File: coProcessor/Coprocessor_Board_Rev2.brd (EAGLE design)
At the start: 101.6 x 101.6 mm, 95 parts, among them IC1 STM32F405RGT6, J1 USB_MINI-B_SMT, J4 30320-6002HB, J5 5008730806, Q1 L78M05CV, U1 MAX3051ESA

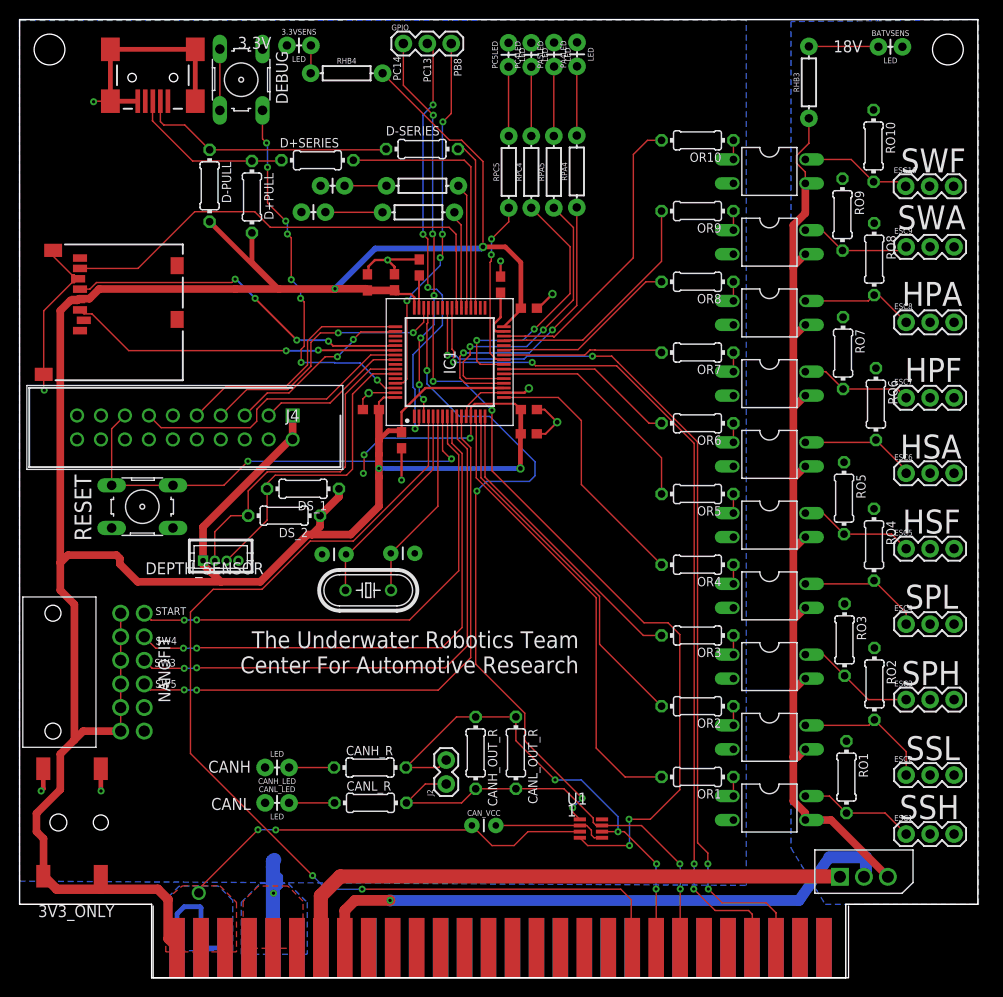
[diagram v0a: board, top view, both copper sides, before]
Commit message: fixed led orientation, added switch to switch connector
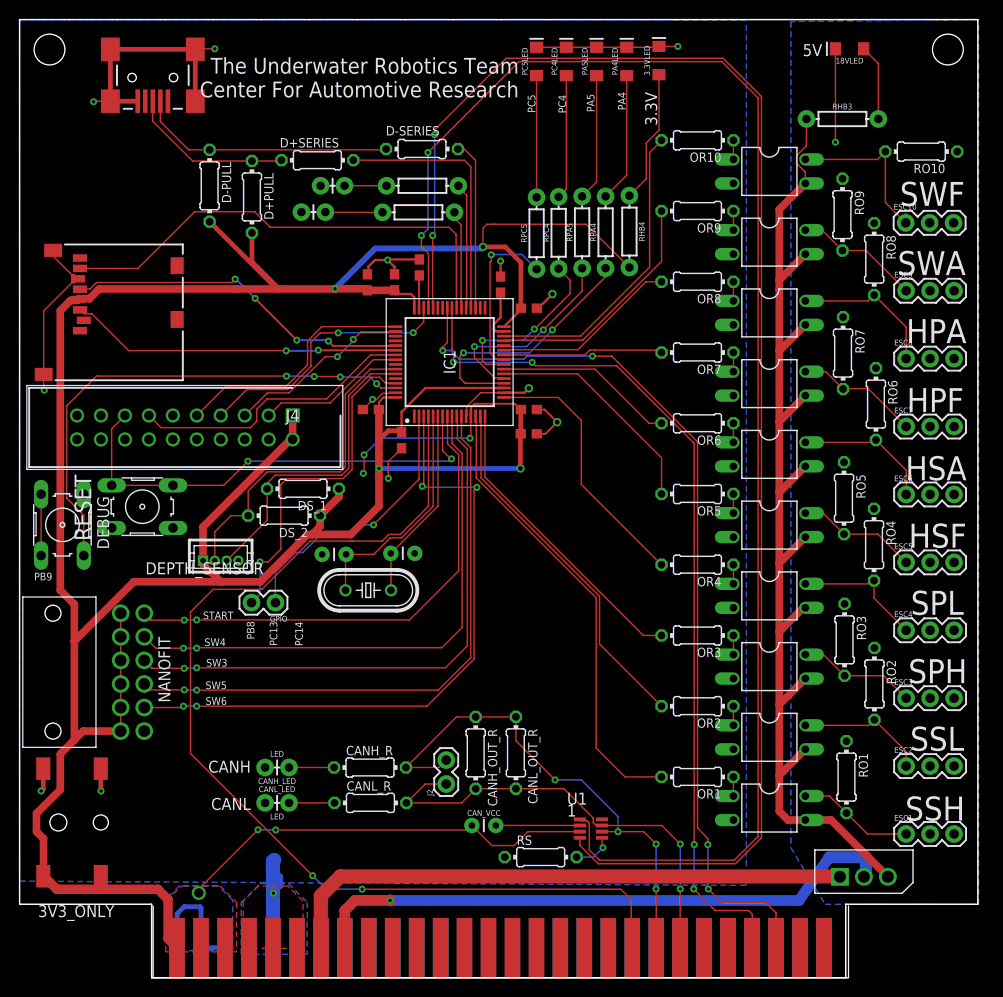
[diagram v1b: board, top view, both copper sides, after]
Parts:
- removed 3.3VSENS, BATVSENS: LED, SparkFun-Resistors:AXIAL-0.1
- added 18VLED, 3.3VLED: WHITE, SparkFun-LED:LED-1206
- added RS: 0, resistor:0204/7
- C10, C2, C3, C4, C5: value 100 nF -> .1 uF
- GPIO: device SparkFun-Connectors:1X03 -> SparkFun-Connectors:1X02
- PA4LED, PA5LED, PC4LED, PC5LED: value LED -> WHITE; device SparkFun-Resistors:AXIAL-0.1 -> SparkFun-LED:LED-1206
- RHB3: value 1.5k -> 1.8k
- RHB4, RPA4, RPA5, RPC4, RPC5: value 1k -> 330
- moved GPIO 60.8 mm to (27.1, 39.8), turned to 180 degrees
- moved DEBUG 50.9 mm to (4.54, 48.0)
- moved RHB4 34.4 mm to (64.7, 79.1), turned to 270 degrees
- moved RPC5 7.14 mm to (54.8, 78.9)
- moved RPA4 7.13 mm to (62.1, 79.0)
- moved RPC4 7.07 mm to (57.2, 79.0)
- moved RPA5 7.07 mm to (59.6, 79.0)
- moved PA4LED 5.33 mm to (64.4, 97.2)
- moved RHB3 5.26 mm to (87.2, 91.1), turned to 0 degrees
- moved RO10 5.10 mm to (95.6, 87.6), turned to 180 degrees
- moved ESC9 4.65 mm to (94.0, 72.8)
- moved PA5LED 4.57 mm to (61.2, 97.2)
- moved ESC10 3.88 mm to (93.9, 80.0)
- moved ESC8 3.85 mm to (94.0, 65.7)
- moved PC4LED 3.78 mm to (58.0, 97.2)
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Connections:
- net N$12 renamed PB9
- removed net GNDA: BATVSENS.P$2
- removed net PC14: GPIO.1, IC1.3
- new net N$2: RS.2, U1.8
- new net SWITCH6: IC1.3, U$2.CK2
- net GND: now also 3.3VLED.C, PA4LED.C, PA5LED.C, PC4LED.C, PC5LED.C, RS.1; no longer 3.3VSENS.P$1, PA4LED.P$2, PA5LED.P$2, PC4LED.P$2, PC5LED.P$2, U1.8
- net GNDBAT: now also 18VLED.C
- net N$10: now also PC4LED.A; no longer PC4LED.P$1
- net N$11: now also PC5LED.A; no longer PC5LED.P$1
- net N$3: now also 18VLED.A; no longer BATVSENS.P$1
- net N$4: now also 3.3VLED.A; no longer 3.3VSENS.P$2
- net N$7: now also PA4LED.A; no longer PA4LED.P$1
- net N$8: now also PA5LED.A; no longer PA5LED.P$1
- net PB8: now also GPIO.2; no longer GPIO.3
- net PC13: now also GPIO.1; no longer GPIO.2
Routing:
- net CAN1_TXD: track 71.6 -> 159.4 mm, vias 4 -> 2
- net CAN1_RXD: track 80.4 -> 159.0 mm, vias 4 -> 2
- net SWITCH6: track 0.00 -> 68.8 mm, vias 0 -> 4
- net PC14: track 41.8 -> 0.00 mm, vias 6 -> 0
- net 5V: track 101.8 -> 120.9 mm
- net PC13: track 45.7 -> 29.2 mm, vias 4 -> 1
- net GND: track 109.5 -> 123.8 mm, vias 12 -> 14
- net PB9: track 39.8 -> 53.3 mm, vias 8 -> 4
- net N$4: track 2.96 -> 14.1 mm
- net HEARTBEAT_4: track 31.4 -> 21.5 mm
- net GNDBAT: track 64.2 -> 74.1 mm, vias 1 -> 2
- net PC4: track 28.0 -> 19.1 mm
- net PWM5V10: track 11.8 -> 18.2 mm
- net N$7: track 7.35 -> 13.7 mm
- net N$8: track 7.38 -> 13.4 mm
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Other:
- board text added: "5V"
- board text added: "PA4"
- board text added: "PA5"
- board text added: "PB9"
- board text added: "PC4"
- board text added: "PC5"
- board text added: "SW6"
- board text removed: "18V"

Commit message: General cleanup (salutes) of the converter and copro eagle files
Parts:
- moved 3.3VLED 14.2 mm to (53.6, 97.1)
- moved RHB4 13.6 mm to (51.6, 82.9)
- moved PC5LED 11.6 mm to (66.4, 97.0)
- moved RPC5 9.50 mm to (64.3, 79.1)
- moved PA4LED 7.62 mm to (56.8, 97.0)
- moved RPA4 6.96 mm to (55.2, 79.1)
- moved DS_2 6.89 mm to (34.3, 51.9)
- moved PC4LED 5.18 mm to (63.2, 97.0)
- moved DS_1 4.86 mm to (34.2, 49.3)
- moved RPC4 4.11 mm to (61.3, 79.1)
- moved OSCILLATOR 3.06 mm to (40.0, 40.8)
- moved C8 3.05 mm to (36.4, 44.7)
- moved C9 3.05 mm to (43.7, 44.9)
- moved C2 1.91 mm to (38.1, 72.8)
- moved HBL2 1.68 mm to (29.5, 81.2)
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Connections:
- removed net N$9: DEBUG.3, DEBUG.4
- net GND: now also DEBUG.3, DEBUG.4
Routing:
- net HEARTBEAT_3: track 27.0 -> 74.8 mm, vias 2 -> 1
- net HEARTBEAT_4: track 21.5 -> 68.7 mm, vias 2 -> 1
- net 3.3V: track 408.5 -> 366.7 mm, vias 10 -> 5
- net KILLSWITCH: track 112.7 -> 71.0 mm, vias 2 -> 4
- net PC4: track 19.1 -> 41.2 mm, vias 2 -> 1
- net PC5: track 17.7 -> 34.4 mm
- net SDA_BKPLN: track 93.5 -> 84.4 mm
- net SCL_BKPLN: track 95.8 -> 87.1 mm
- net N$9: track 6.50 -> 0.00 mm
- net N$4: track 14.1 -> 9.71 mm
- net RCC_OSC_IN: track 24.7 -> 21.3 mm
- net PB8: track 36.0 -> 32.6 mm
- net DEPTHSCL: track 35.4 -> 33.1 mm
- net GND: track 123.8 -> 125.7 mm
- net SYS_JTDI: track 28.6 -> 26.7 mm
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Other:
- board text added: "The Ohio State University Center For Automotive Research The Underwater Robotics Team CoProcessor Board -- Rev 2.0"
- board text removed: "PB9"
- board text removed: "The Underwater Robotics Team Center For Automotive Research"
